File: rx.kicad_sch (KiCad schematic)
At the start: 53 parts, among them J13 RFShield_Frame, J5 SWH, J7 SMA, J9 SWH, T1 RF_BALUN, T1 RXIF_BALUN, U14 MAX2120, U16 DPDT

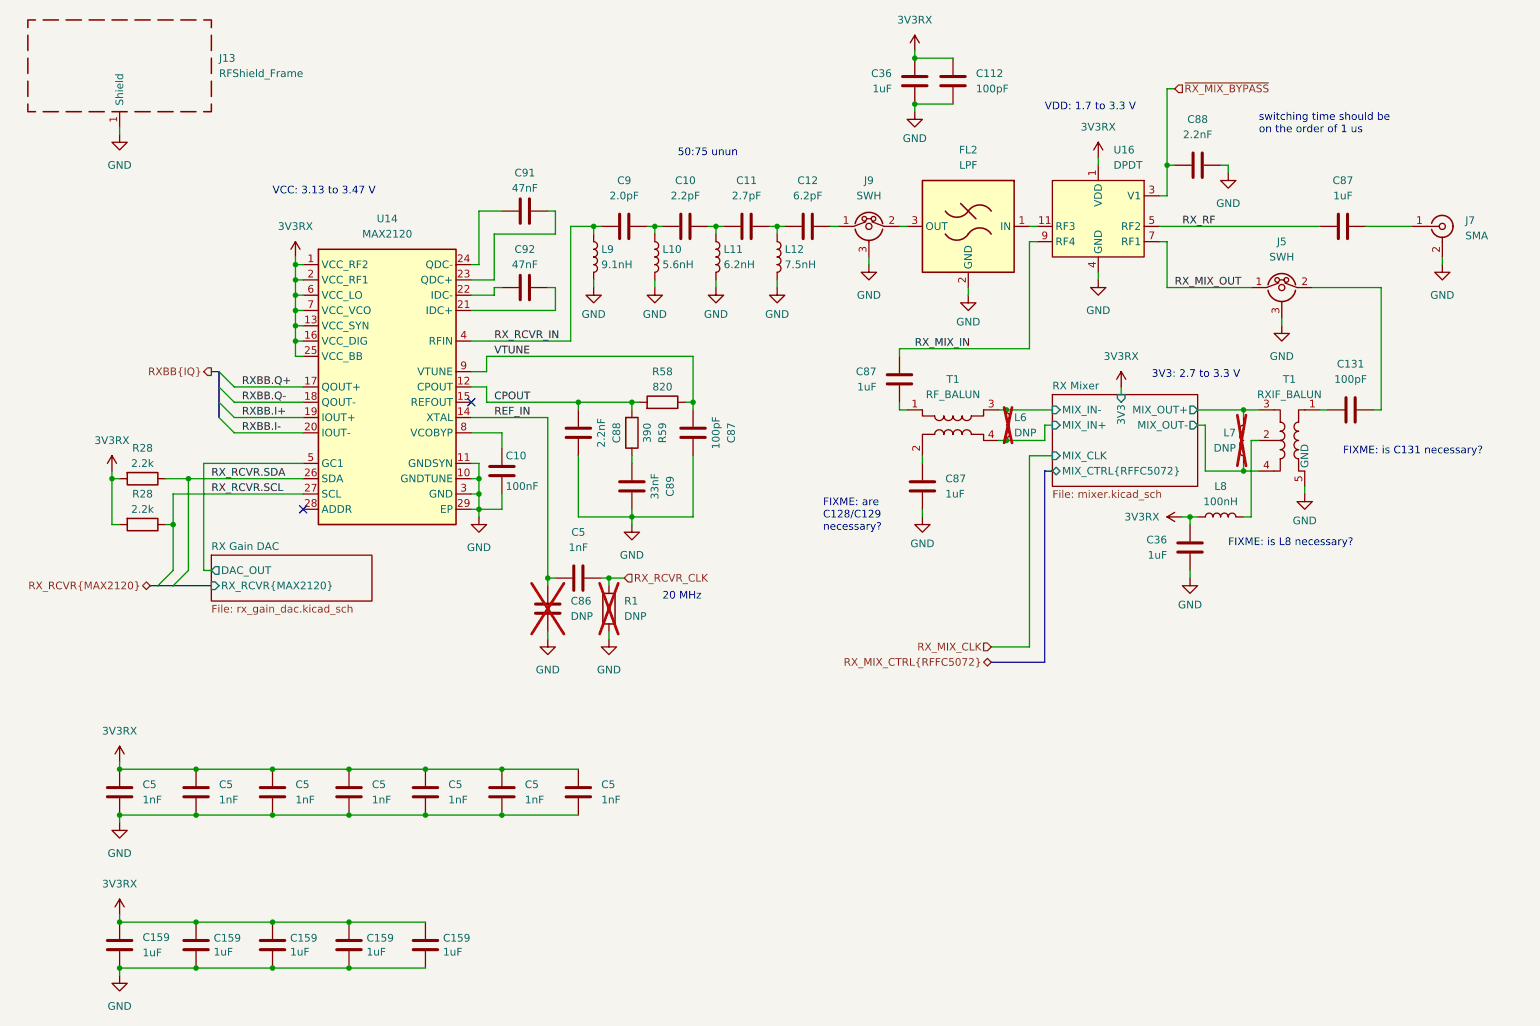
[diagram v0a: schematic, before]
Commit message: Replace open drain clock inverters with push-pull
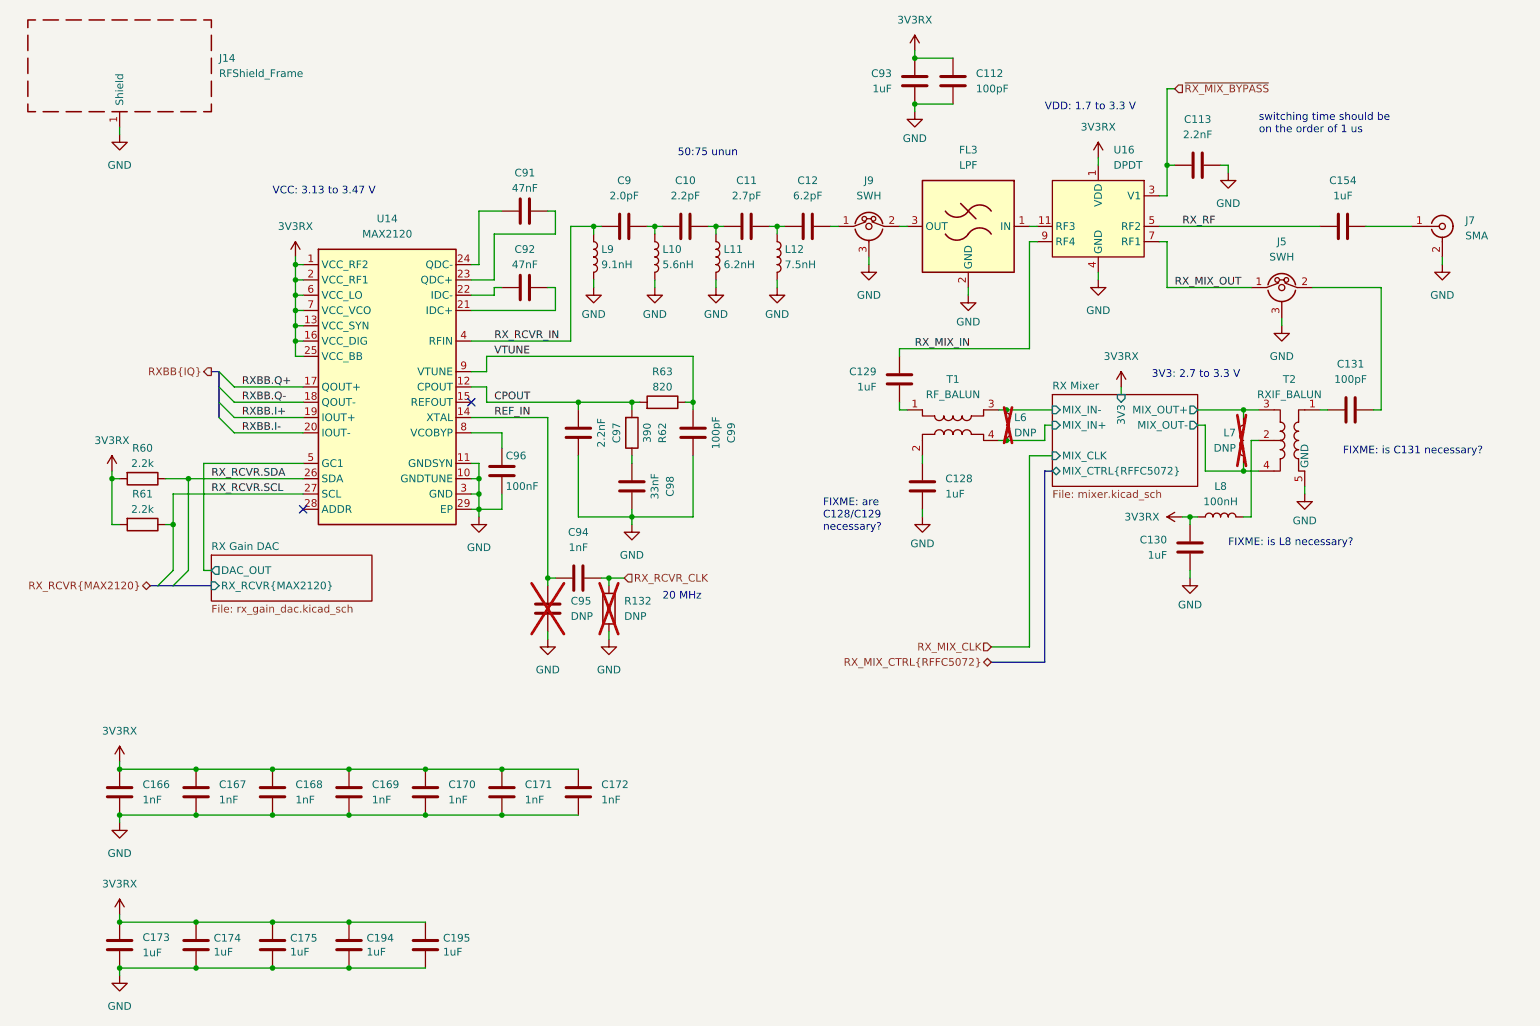
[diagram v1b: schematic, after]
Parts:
- renumbered C88 to C113, C87 to C128, C87 to C129, C36 to C130, C87 to C154, C5 to C166, C5 to C167, C5 to C168, C5 to C169, C5 to C170, C5 to C171, C5 to C172, C159 to C173, C159 to C174, C159 to C175, C159 to C194, C159 to C195, C36 to C93, C5 to C94, C86 to C95, C10 to C96, C88 to C97, C89 to C98, C87 to C99, FL2 to FL3, J13 to J14, R1 to R132, R28 to R60, R28 to R61, R59 to R62, R58 to R63, T1 to T2

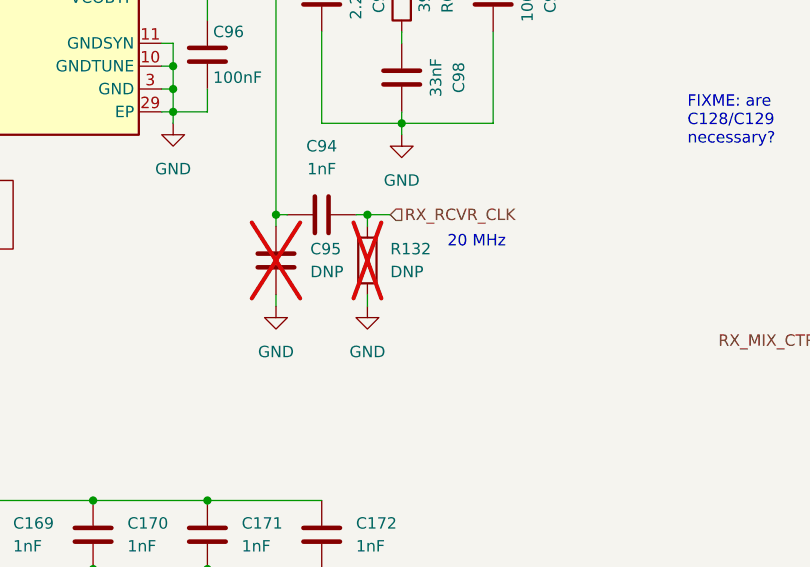
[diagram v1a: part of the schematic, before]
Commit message: Tune clock passives
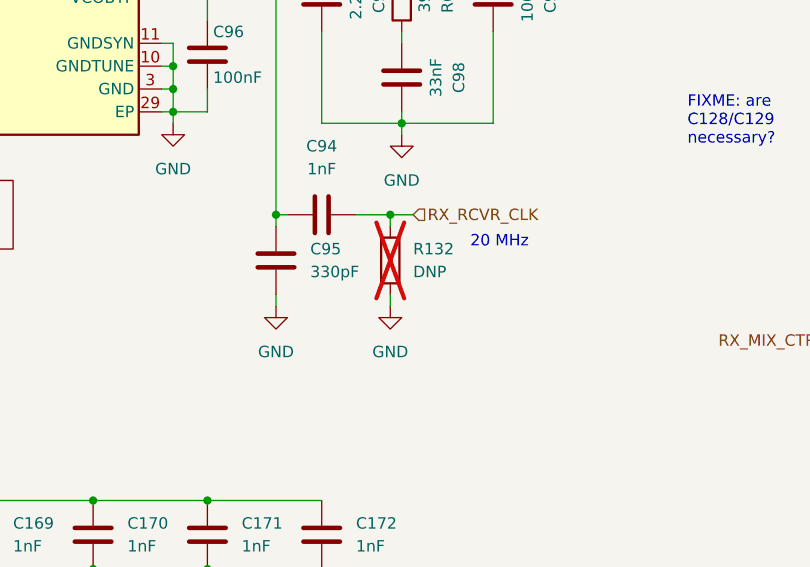
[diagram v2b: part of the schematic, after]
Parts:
- C95: value DNP -> 330pF; Manufacturer (none) -> Murata; Part Number (none) -> GRM0335C1E331JA01D; Substitution (none) -> GRM0335C1E331JA01*; now fitted
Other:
- moved on the sheet: R132
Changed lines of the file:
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@@
   (junction (at 147.32 57.15) (diameter 0) (color 0 0 0 0)
   )
-  (junction (at 119.38 115.57) (diameter 0) (color 0 0 0 0)
+  (junction (at 121.92 115.57) (diameter 0) (color 0 0 0 0)
   )
   (junction (at 49.53 99.06) (diameter 0) (color 0 0 0 0)
@@
     (stroke (width 0) (type default))
   )
-  (wire (pts (xy 119.38 115.57) (xy 119.38 116.84))
+  (wire (pts (xy 121.92 115.57) (xy 121.92 116.84))
     (stroke (width 0) (type default))
   )
@@
     (stroke (width 0) (type default))
   )
-  (wire (pts (xy 119.38 115.57) (xy 121.92 115.57))
+  (wire (pts (xy 121.92 115.57) (xy 124.46 115.57))
     (stroke (width 0) (type default))
   )
@@
     (stroke (width 0) (type default))
   )
-  (wire (pts (xy 119.38 124.46) (xy 119.38 125.73))
+  (wire (pts (xy 121.92 124.46) (xy 121.92 125.73))
     (stroke (width 0) (type default))
   )
@@
     (stroke (width 0) (type default))
   )
-  (wire (pts (xy 118.11 115.57) (xy 119.38 115.57))
+  (wire (pts (xy 118.11 115.57) (xy 121.92 115.57))
     (stroke (width 0) (type default))
   )
@@
     (stroke (width 0) (type default))
   )
-  (text "20 MHz" (at 128.27 119.38 0)
+  (text "20 MHz" (at 130.81 119.38 0)
     (effects (font (size 1.27 1.27)) (justify left bottom))
   )
@@
     (effects (font (size 1.27 1.27)) (justify right))
   )
-  (hierarchical_label "RX_RCVR_CLK" (shape input) (at 121.92 115.57 0) (fields_autoplaced)
+  (hierarchical_label "RX_RCVR_CLK" (shape input) (at 124.46 115.57 0) (fields_autoplaced)
     (effects (font (size 1.27 1.27)) (justify left))
   )
@@
   )
   (symbol (lib_id "Device:C") (at 109.22 120.65 0) (unit 1)
-    (in_bom yes) (on_board yes) (dnp yes) (fields_autoplaced)
+    (in_bom yes) (on_board yes) (dnp no) (fields_autoplaced)
     (property "Reference" "C95" (at 113.03 119.38 0)
       (effects (font (size 1.27 1.27)) (justify left))
     )
-    (property "Value" "DNP" (at 113.03 121.92 0)
+    (property "Value" "330pF" (at 113.03 121.92 0)
       (effects (font (size 1.27 1.27)) (justify left))
     )
@@
       (effects (font (size 1.27 1.27)) hide)
     )
+    (property "Description" "CAP CER 330PF 25V C0G/NP0 0201" (at 109.22 120.65 0)
+      (effects (font (size 1.27 1.27)) hide)
+    )
+    (property "Manufacturer" "Murata" (at 109.22 120.65 0)
+      (effects (font (size 1.27 1.27)) hide)
+    )
+    (property "Part Number" "GRM0335C1E331JA01D" (at 109.22 120.65 0)
+      (effects (font (size 1.27 1.27)) hide)
+    )
+    (property "Substitution" "GRM0335C1E331JA01*" (at 109.22 120.65 0)
+      (effects (font (size 1.27 1.27)) hide)
+    )
     (pin "1")
     (pin "2")
@@
     )
   )
-  (symbol (lib_id "Device:R") (at 119.38 120.65 0) (unit 1)
+  (symbol (lib_id "Device:R") (at 121.92 120.65 0) (unit 1)
     (in_bom yes) (on_board yes) (dnp yes) (fields_autoplaced)
-    (property "Reference" "R132" (at 121.92 119.38 0)
+    (property "Reference" "R132" (at 124.46 119.38 0)
       (effects (font (size 1.27 1.27)) (justify left))
     )
-    (property "Value" "DNP" (at 121.92 121.92 0)
+    (property "Value" "DNP" (at 124.46 121.92 0)
       (effects (font (size 1.27 1.27)) (justify left))
     )
-    (property "Footprint" "Resistor_SMD:R_0402_1005Metric" (at 117.602 120.65 90)
+    (property "Footprint" "Resistor_SMD:R_0402_1005Metric" (at 120.142 120.65 90)
       (effects (font (size 1.27 1.27)) hide)
     )
-    (property "Datasheet" "~" (at 119.38 120.65 0)
+    (property "Datasheet" "~" (at 121.92 120.65 0)
       (effects (font (size 1.27 1.27)) hide)
     )
-    (property "Part Number" "" (at 119.38 120.65 0)
+    (property "Part Number" "" (at 121.92 120.65 0)
       (effects (font (size 1.27 1.27)) hide)
     )
-    (property "Substitution" "" (at 119.38 120.65 0)
+    (property "Substitution" "" (at 121.92 120.65 0)
       (effects (font (size 1.27 1.27)) hide)
     )
-    (property "Description" "" (at 119.38 120.65 0)
+    (property "Description" "" (at 121.92 120.65 0)
       (effects (font (size 1.27 1.27)) hide)
     )
-    (property "Manufacturer" "" (at 119.38 120.65 0)
+    (property "Manufacturer" "" (at 121.92 120.65 0)
       (effects (font (size 1.27 1.27)) hide)
     )
@@
     )
   )
-  (symbol (lib_id "power:GND") (at 119.38 125.73 0) (unit 1)
+  (symbol (lib_id "power:GND") (at 121.92 125.73 0) (unit 1)
     (in_bom yes) (on_board yes) (dnp no) (fields_autoplaced)
-    (property "Reference" "#PWR0341" (at 119.38 132.08 0)
+    (property "Reference" "#PWR0341" (at 121.92 132.08 0)
       (effects (font (size 1.27 1.27)) hide)
     )
-    (property "Value" "GND" (at 119.38 130.81 0)
+    (property "Value" "GND" (at 121.92 130.81 0)
       (effects (font (size 1.27 1.27)))
     )
-    (property "Footprint" "" (at 119.38 125.73 0)
+    (property "Footprint" "" (at 121.92 125.73 0)
       (effects (font (size 1.27 1.27)) hide)
     )
-    (property "Datasheet" "" (at 119.38 125.73 0)
+    (property "Datasheet" "" (at 121.92 125.73 0)
       (effects (font (size 1.27 1.27)) hide)
     )
